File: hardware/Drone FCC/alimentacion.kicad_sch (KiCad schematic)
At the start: 14 parts, among them J901 PM02 PixHawk, U901 ZLDO1117QG33TA

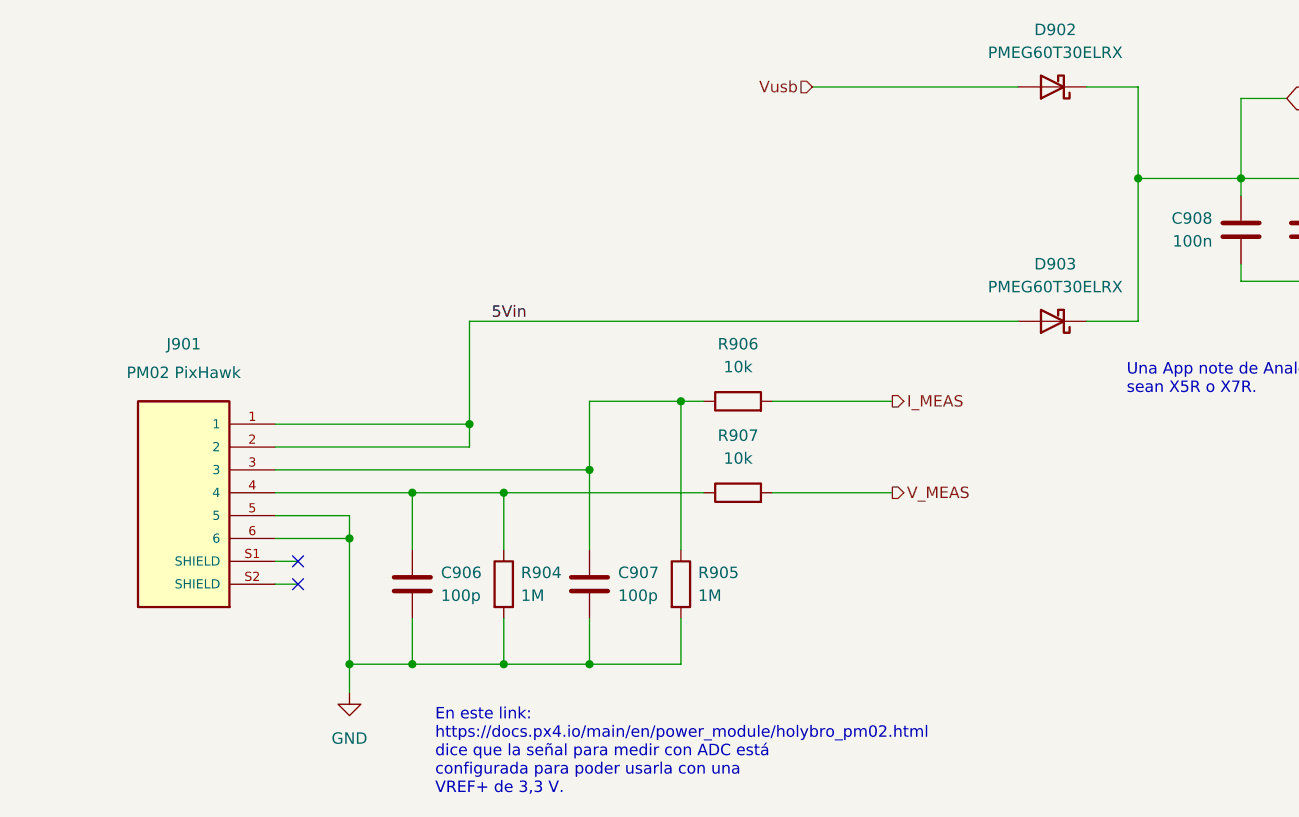
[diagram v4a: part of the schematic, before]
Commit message: added missing TVS diodes
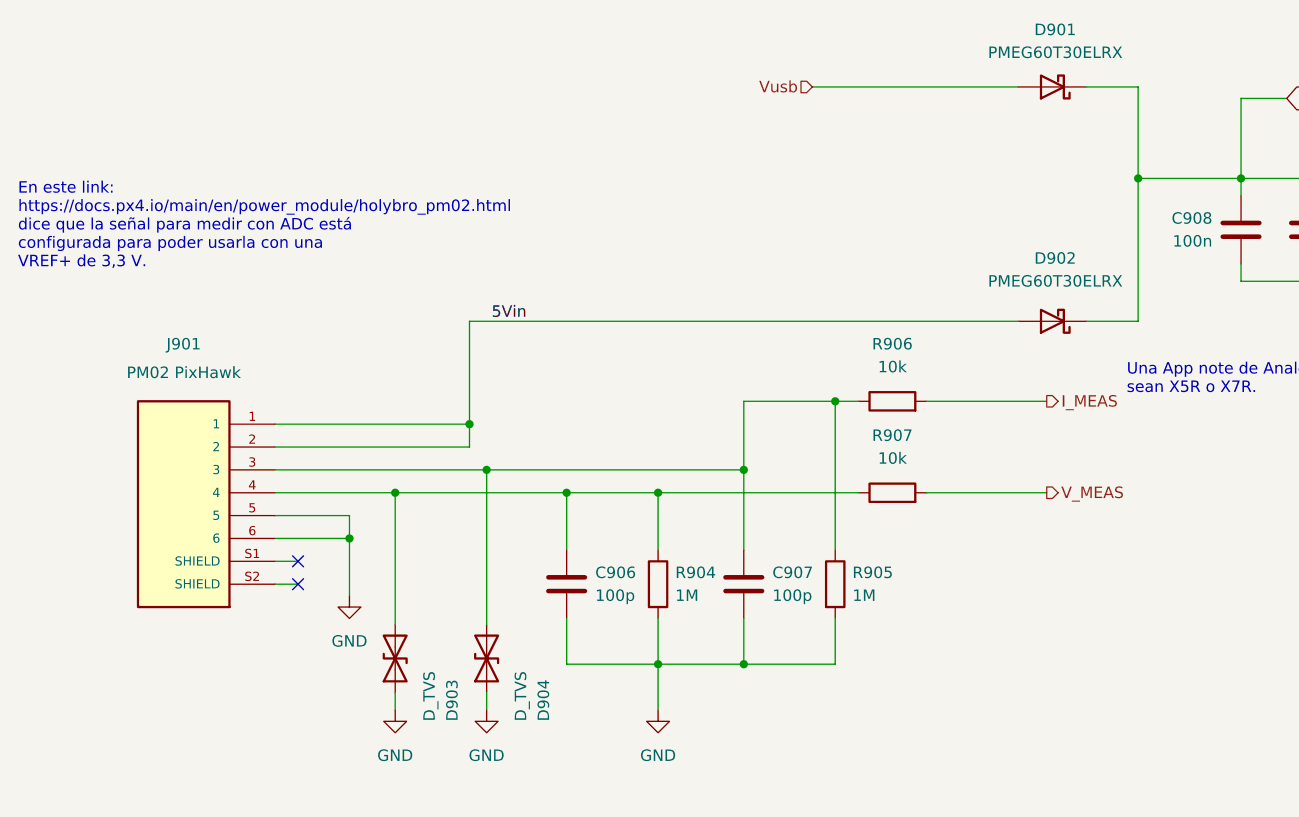
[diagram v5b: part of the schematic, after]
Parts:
- added D903, D904: D_TVS, Diode_SMD:D_0402_1005Metric_Pad0.77x0.64mm_HandSolder, symbol Device:D_TVS
- renumbered D902 to D901, D903 to D902
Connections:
- net GND: now also D903.1 (A1), D904.1 (A1)
- net at C906.1, J901.4, R904.1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: now also D903.2 (A2)
- net at C907.1, J901.3, R905.1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: now also D904.2 (A2)
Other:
- moved on the sheet: C906, C907, R904, R905, R906, R907

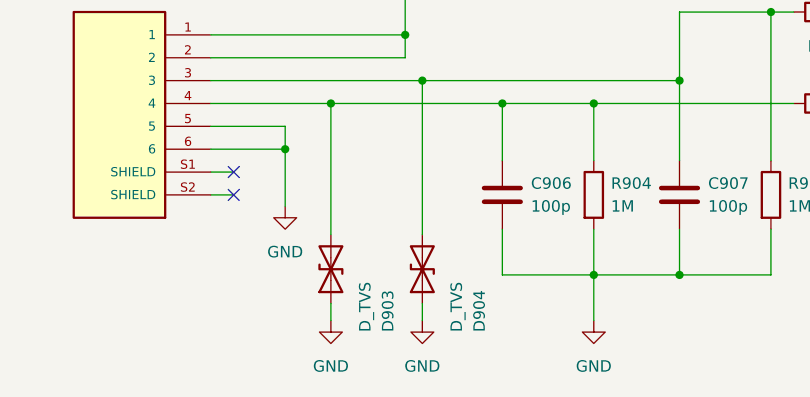
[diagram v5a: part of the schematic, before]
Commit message: removed all the TVS from the PCB and SCH
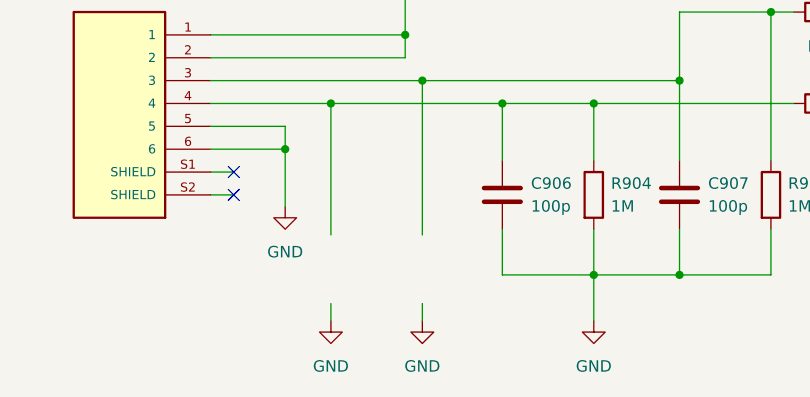
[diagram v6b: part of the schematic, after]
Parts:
- removed D903, D904: D_TVS, Diode_SMD:D_0402_1005Metric_Pad0.77x0.64mm_HandSolder, symbol Device:D_TVS
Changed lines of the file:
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@@
     (effects (font (size 1.27 1.27)) (justify left))
-  )
-  (symbol (lib_id "Device:D_TVS") (at 81.915 119.38 90) (unit 1)
-    (in_bom yes) (on_board yes)
-    (property "Reference" "D904" (id 0) (at 88.265 126.365 0)
-      (effects (font (size 1.27 1.27)) (justify left))
-    )
-    (property "Value" "D_TVS" (id 1) (at 85.725 126.365 0)
-      (effects (font (size 1.27 1.27)) (justify left))
-    )
-    (property "Footprint" "Diode_SMD:D_0402_1005Metric_Pad0.77x0.64mm_HandSolder" (id 2) (at 81.915 119.38 0)
-      (effects (font (size 1.27 1.27)) hide)
-    )
-    (property "Datasheet" "~" (id 3) (at 81.915 119.38 0)
-      (effects (font (size 1.27 1.27)) hide)
-    )
-    (pin "1")
-    (pin "2")
   )
   (symbol (lib_id "Device:R") (at 127 100.965 90) (unit 1)
@@
       (effects (font (size 1.27 1.27)) hide)
     )
-    (pin "1")
-    (pin "2")
-  )
-  (symbol (lib_id "Device:D_TVS") (at 71.755 119.38 90) (unit 1)
-    (in_bom yes) (on_board yes)
-    (property "Reference" "D903" (id 0) (at 78.105 126.365 0)
-      (effects (font (size 1.27 1.27)) (justify left))
-    )
-    (property "Value" "D_TVS" (id 1) (at 75.565 126.365 0)
-      (effects (font (size 1.27 1.27)) (justify left))
-    )
-    (property "Footprint" "Diode_SMD:D_0402_1005Metric_Pad0.77x0.64mm_HandSolder" (id 2) (at 71.755 119.38 0)
-      (effects (font (size 1.27 1.27)) hide)
-    )
-    (property "Datasheet" "~" (id 3) (at 71.755 119.38 0)
-      (effects (font (size 1.27 1.27)) hide)
-    )

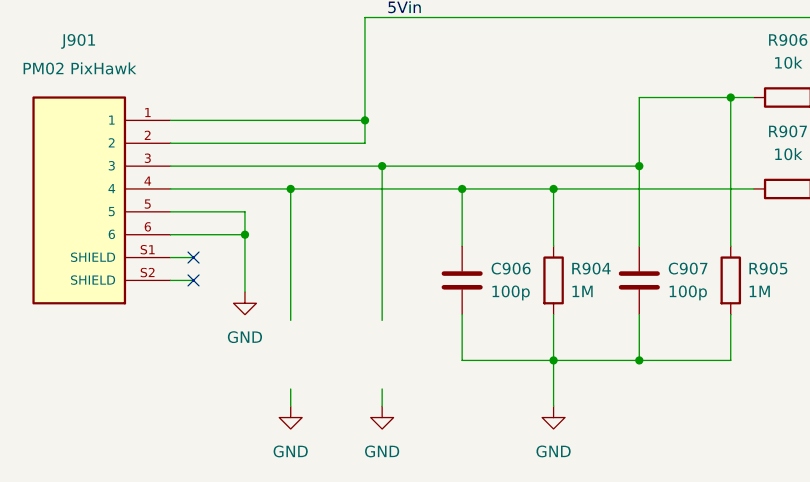
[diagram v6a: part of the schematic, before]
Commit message: tidying up the schematic
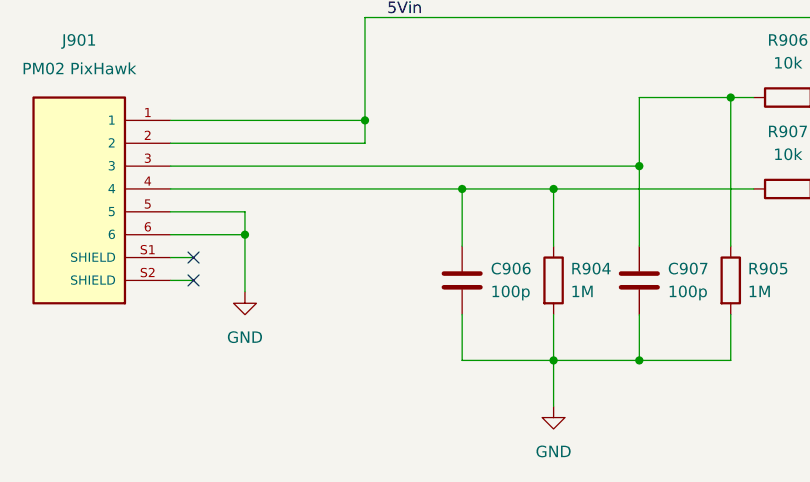
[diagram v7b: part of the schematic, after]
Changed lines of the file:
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@@
   (junction (at 213.995 66.04) (diameter 0) (color 0 0 0 0)
   )
-  (junction (at 81.915 98.425) (diameter 0) (color 0 0 0 0)
-  )
   (junction (at 201.295 66.04) (diameter 0) (color 0 0 0 0)
   )
@@
   )
   (junction (at 154.305 66.04) (diameter 0) (color 0 0 0 0)
-  )
-  (junction (at 71.755 100.965) (diameter 0) (color 0 0 0 0)
   )
   (junction (at 110.49 120.015) (diameter 0) (color 0 0 0 0)
@@
     (stroke (width 0) (type default) (color 0 0 0 0))
   )
-  (wire (pts (xy 81.915 98.425) (xy 110.49 98.425))
-    (stroke (width 0) (type default) (color 0 0 0 0))
-  )
   (wire (pts (xy 187.325 77.47) (xy 201.295 77.47))
     (stroke (width 0) (type default) (color 0 0 0 0))
@@
     (stroke (width 0) (type default) (color 0 0 0 0))
   )
-  (wire (pts (xy 71.755 100.965) (xy 90.805 100.965))
-    (stroke (width 0) (type default) (color 0 0 0 0))
-  )
-  (wire (pts (xy 81.915 98.425) (xy 81.915 115.57))
+  (wire (pts (xy 58.42 100.965) (xy 90.805 100.965))
     (stroke (width 0) (type default) (color 0 0 0 0))
   )
@@
     (stroke (width 0) (type default) (color 0 0 0 0))
   )
-  (wire (pts (xy 81.915 123.19) (xy 81.915 125.095))
-    (stroke (width 0) (type default) (color 0 0 0 0))
-  )
   (wire (pts (xy 80.01 93.345) (xy 80.01 95.885))
     (stroke (width 0) (type default) (color 0 0 0 0))
@@
     (stroke (width 0) (type default) (color 0 0 0 0))
   )
-  (wire (pts (xy 58.42 98.425) (xy 81.915 98.425))
+  (wire (pts (xy 58.42 98.425) (xy 110.49 98.425))
     (stroke (width 0) (type default) (color 0 0 0 0))
   )
@@
     (stroke (width 0) (type default) (color 0 0 0 0))
   )
-  (wire (pts (xy 58.42 100.965) (xy 71.755 100.965))
-    (stroke (width 0) (type default) (color 0 0 0 0))
-  )
   (wire (pts (xy 120.65 90.805) (xy 123.19 90.805))
     (stroke (width 0) (type default) (color 0 0 0 0))
@@
     (stroke (width 0) (type default) (color 0 0 0 0))
   )
-  (wire (pts (xy 71.755 100.965) (xy 71.755 115.57))
-    (stroke (width 0) (type default) (color 0 0 0 0))
-  )
   (wire (pts (xy 58.42 95.885) (xy 80.01 95.885))
     (stroke (width 0) (type default) (color 0 0 0 0))
@@
   )
   (wire (pts (xy 165.735 66.04) (xy 173.355 66.04))
-    (stroke (width 0) (type default) (color 0 0 0 0))
-  )
-  (wire (pts (xy 71.755 123.19) (xy 71.755 125.095))
     (stroke (width 0) (type default) (color 0 0 0 0))
   )
@@
     (pin "1")
     (pin "2")
-  )
-  (symbol (lib_id "power:GND") (at 81.915 125.095 0) (mirror y) (unit 1)
-    (in_bom yes) (on_board yes) (fields_autoplaced)
-    (property "Reference" "#PWR0246" (id 0) (at 81.915 131.445 0)
-      (effects (font (size 1.27 1.27)) hide)
-    )
-    (property "Value" "GND" (id 1) (at 81.915 130.175 0))
-    (property "Footprint" "" (id 2) (at 81.915 125.095 0)
-      (effects (font (size 1.27 1.27)) hide)
-    )
-    (property "Datasheet" "" (id 3) (at 81.915 125.095 0)
-      (effects (font (size 1.27 1.27)) hide)
-    )
-    (pin "1")
   )
   (symbol (lib_id "Device:C") (at 213.995 71.755 0) (unit 1)
@@
       (effects (font (size 1.27 1.27)) hide)
     )
-    (pin "1")
-  )
-  (symbol (lib_id "power:GND") (at 71.755 125.095 0) (mirror y) (unit 1)
-    (in_bom yes) (on_board yes) (fields_autoplaced)
-    (property "Reference" "#PWR0245" (id 0) (at 71.755 131.445 0)
-      (effects (font (size 1.27 1.27)) hide)
-    )
-    (property "Value" "GND" (id 1) (at 71.755 130.175 0))
-    (property "Footprint" "" (id 2) (at 71.755 125.095 0)
-      (effects (font (size 1.27 1.27)) hide)
-    )
-    (property "Datasheet" "" (id 3) (at 71.755 125.095 0)
-      (effects (font (size 1.27 1.27)) hide)
-    )
